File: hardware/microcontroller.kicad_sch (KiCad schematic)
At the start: 50 parts, among them J301 TC2050, J302 61300611121, J303 61300611121, J304 61300611121, J305 61300611121, J306 61300611121, J307 61300611121, Q301 BSS806NH, SW301 430182050816, SW302 430182050816, U301 STM32L552CET6, Y301 ECS-160-9-37-CKM-TR3, Y302 ABS05-32.768KHZ-9-T

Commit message: HW: Use 0201 where applicable
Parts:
- removed R319: 2.2 kΩ, perfect_footprints:R_0402_1005Metric, symbol Device:R
- added R305: 2.2 kΩ, perfect_footprints:R_0201_0603Metric, symbol Device:R
- C301, C302, C304, C305, C306, C307, C308, C309, C310, C311, C312, C313, C315: footprint perfect_footprints:C_0402_1005Metric -> perfect_footprints:C_0201_0603Metric; Size 0402 -> 0201
- C303, C314: value 4.7 µF -> 22 µF; footprint perfect_footprints:C_0402_1005Metric_HDI -> Capacitor_SMD:C_0603_1608Metric; Size 0402 -> 0603
- R301, R302: footprint perfect_footprints:R_0402_1005Metric -> perfect_footprints:R_0201_0603Metric; Power rating 0.1 W -> 0.05 W; Size 0402 -> 0201
- R303: renamed from R304; footprint perfect_footprints:R_0402_1005Metric -> perfect_footprints:R_0201_0603Metric; Power rating 0.1 W -> 0.05 W; Size 0402 -> 0201
- R304: renamed from R303; footprint perfect_footprints:R_0402_1005Metric -> perfect_footprints:R_0201_0603Metric; Power rating 0.1 W -> 0.05 W; Size 0402 -> 0201
- R306: renamed from R321; footprint perfect_footprints:R_0402_1005Metric -> perfect_footprints:R_0201_0603Metric; Power rating 0.1 W -> 0.05 W; Size 0402 -> 0201
- R307: renamed from R305; footprint perfect_footprints:R_0402_1005Metric -> perfect_footprints:R_0201_0603Metric; Power rating 0.1 W -> 0.05 W; Size 0402 -> 0201
- R308: renamed from R306; footprint perfect_footprints:R_0402_1005Metric -> perfect_footprints:R_0201_0603Metric; Power rating 0.1 W -> 0.05 W; Size 0402 -> 0201
- R309: renamed from R307; footprint perfect_footprints:R_0402_1005Metric -> perfect_footprints:R_0201_0603Metric; Power rating 0.1 W -> 0.05W; Size 0402 -> 0201
- R310: renamed from R308; footprint perfect_footprints:R_0402_1005Metric -> perfect_footprints:R_0201_0603Metric; Power rating 0.1 W -> 0.05W; Size 0402 -> 0201
- R311: renamed from R309; footprint perfect_footprints:R_0402_1005Metric -> perfect_footprints:R_0201_0603Metric; Power rating 0.1 W -> 0.05W; Size 0402 -> 0201
- R312: renamed from R310; footprint perfect_footprints:R_0402_1005Metric -> perfect_footprints:R_0201_0603Metric; Power rating 0.1 W -> 0.05W; Size 0402 -> 0201
- R313: renamed from R311; footprint perfect_footprints:R_0402_1005Metric -> perfect_footprints:R_0201_0603Metric; Power rating 0.1 W -> 0.05W; Size 0402 -> 0201
- R314: renamed from R312; footprint perfect_footprints:R_0402_1005Metric -> perfect_footprints:R_0201_0603Metric; Power rating 0.1 W -> 0.05W; Size 0402 -> 0201
- R315: renamed from R313; footprint perfect_footprints:R_0402_1005Metric -> perfect_footprints:R_0201_0603Metric; Power rating 0.1 W -> 0.05W; Size 0402 -> 0201
- R316: renamed from R314; footprint perfect_footprints:R_0402_1005Metric -> perfect_footprints:R_0201_0603Metric; Power rating 0.1 W -> 0.05W; Size 0402 -> 0201
- R317: renamed from R315; footprint perfect_footprints:R_0402_1005Metric -> perfect_footprints:R_0201_0603Metric; Power rating 0.1 W -> 0.05W; Size 0402 -> 0201
- R319: renamed from R317; footprint perfect_footprints:R_0402_1005Metric -> perfect_footprints:R_0201_0603Metric; Power rating 0.1 W -> 0.05W; Size 0402 -> 0201
- R320: renamed from R318; footprint perfect_footprints:R_0402_1005Metric -> perfect_footprints:R_0201_0603Metric; Power rating 0.1 W -> 0.05 W; Size 0402 -> 0201
- R321: renamed from R320; footprint perfect_footprints:R_0402_1005Metric -> perfect_footprints:R_0201_0603Metric; Power rating 0.1 W -> 0.05 W; Size 0402 -> 0201
- renumbered J304 to J303, J303 to J304, J306 to J305, J305 to J306, R316 to R318
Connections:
- net I2C.SCL: now also J307.3 (Pin_3), R305.2; no longer J307.5 (Pin_5)
- net I2C.SDA: now also J307.5 (Pin_5); no longer J307.3 (Pin_3)
- net V_3V3: now also R305.1
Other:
- note added: "Bulk + 1 µF x VDD pin"
- note removed: "4.7 µF + 1 µF x VDD pin"
- moved on the sheet: C301, C315, J304, J306, R303, R306, R319, SW301, SW302

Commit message: HW: Remove GPIO PA15 and PB2 for easier routing
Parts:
- removed J305: 61300611121, Connector_PinHeader_2.54mm:PinHeader_1x06_P2.54mm_Vertical, symbol Connector_Generic:Conn_01x06
- SW301, SW302: value 430182050816 -> PTS645S
- renumbered C310 to C309, C312 to C310, C313 to C311, C314 to C312, C309 to C313, C311 to C314, J307 to J302, J302 to J303, J303 to J305
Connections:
- net GPIO_PA5: no longer names the net of U301.15 (PA5)
- net GPIO_PB2: no longer names the net of U301.20 (PB2)
- no-connect marks 8 -> 10
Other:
- moved on the sheet: C301, C302, C303, C304, C305, C306, C307, C308, C309, C310, C311, C312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

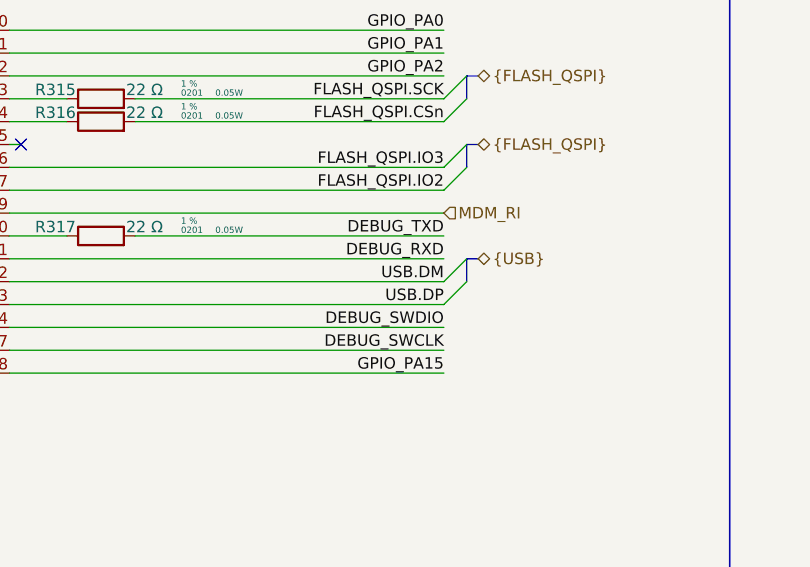
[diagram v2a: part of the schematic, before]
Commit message: HW: Fix BG77, relocate V_BAT bulk cap
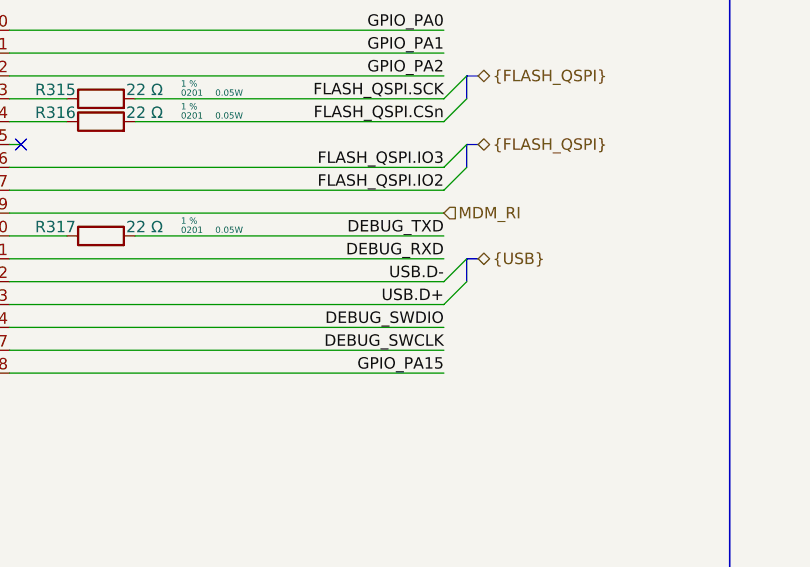
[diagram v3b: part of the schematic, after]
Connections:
- net USB.DM renamed USB.D-
- net USB.DP renamed USB.D+
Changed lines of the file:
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@@
 		)
 	)
-	(label "USB.DM"
+	(label "USB.D-"
 		(at 266.7 111.76 180)
 		(effects
@@
 		)
 	)
-	(label "USB.DP"
+	(label "USB.D+"
 		(at 266.7 114.3 180)
 		(effects

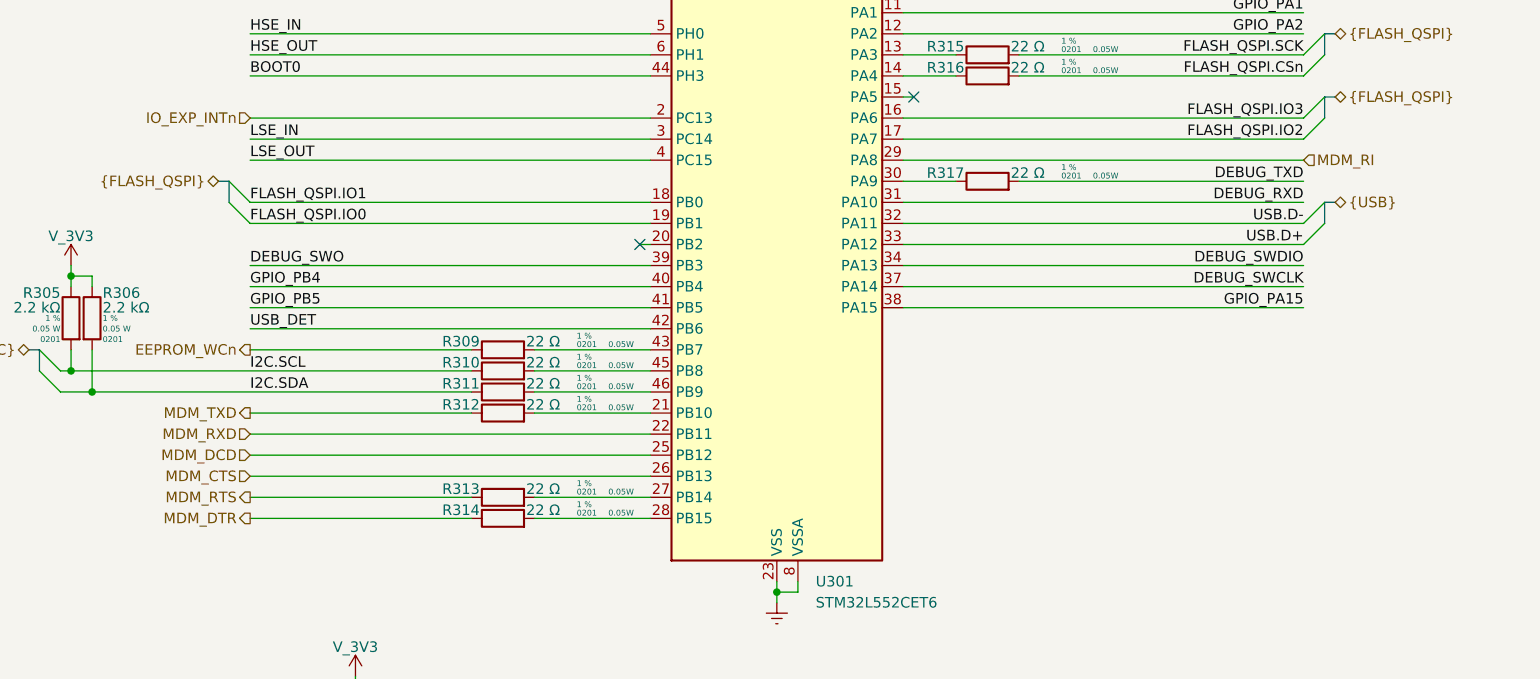
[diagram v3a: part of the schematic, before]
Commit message: HW: Replace BG77 with BG95
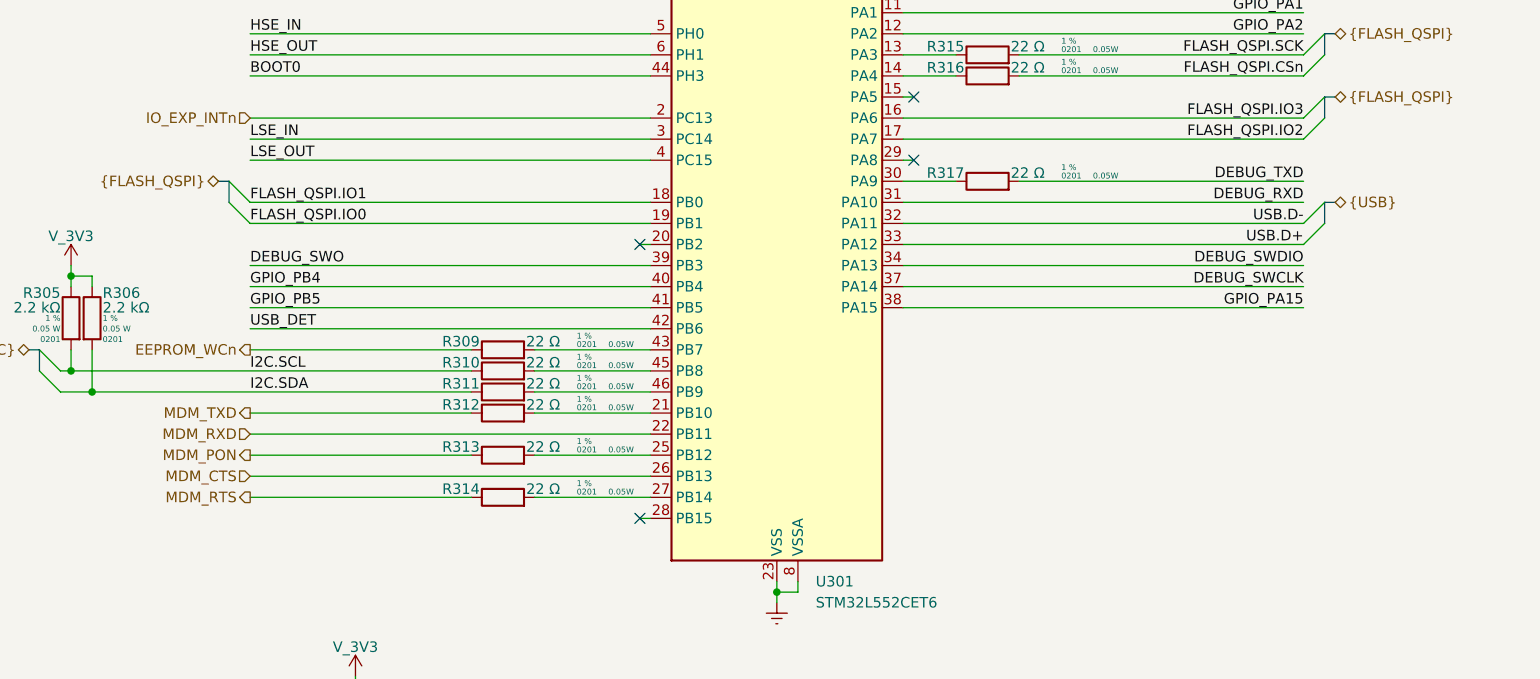
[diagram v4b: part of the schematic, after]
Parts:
- removed R314: 22 Ω, perfect_footprints:R_0201_0603Metric, symbol Device:R
- added R313: 22 Ω, perfect_footprints:R_0201_0603Metric, symbol Device:R
- renumbered R313 to R314
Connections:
- net MDM_DCD: no longer names the net of U301.25 (PB12)
- net MDM_DCD: now also R313.2
- net MDM_RI: no longer names the net of U301.29 (PA8)
- new net MDM_PON: R313.1
- no-connect marks 10 -> 12
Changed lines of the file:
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@@
 	)
 	(no_connect
+		(at 186.69 147.32)
+	)
+	(no_connect
 		(at 43.18 93.98)
 	)
@@
 	)
 	(no_connect
+		(at 219.71 104.14)
+	)
+	(no_connect
 		(at 387.35 97.79)
 	)
@@
 	(wire
 		(pts
-			(xy 173.99 147.32) (xy 187.96 147.32)
-		)
-		(stroke
-			(width 0)
-			(type default)
-		)
-	)
-	(wire
-		(pts
 			(xy 386.08 72.39) (xy 388.62 72.39)
 		)
@@
 	(wire
 		(pts
-			(xy 139.7 139.7) (xy 187.96 139.7)
-		)
-		(stroke
-			(width 0)
-			(type default)
-		)
-	)
-	(wire
-		(pts
 			(xy 254 76.2) (xy 254 77.47)
 		)
@@
 	(wire
 		(pts
+			(xy 139.7 139.7) (xy 166.37 139.7)
+		)
+		(stroke
+			(width 0)
+			(type default)
+		)
+	)
+	(wire
+		(pts
 			(xy 152.4 76.2) (xy 165.1 76.2)
 		)
@@
 	(wire
 		(pts
-			(xy 139.7 147.32) (xy 166.37 147.32)
+			(xy 120.65 127) (xy 120.65 132.08)
 		)
 		(stroke
@@
 	(wire
 		(pts
-			(xy 120.65 127) (xy 120.65 132.08)
+			(xy 190.5 73.66) (xy 190.5 76.2)
 		)
 		(stroke
@@
 	(wire
 		(pts
-			(xy 190.5 73.66) (xy 190.5 76.2)
+			(xy 186.69 147.32) (xy 187.96 147.32)
 		)
 		(stroke
@@
 	(wire
 		(pts
-			(xy 218.44 104.14) (xy 266.7 104.14)
-		)
-		(stroke
-			(width 0)
-			(type default)
-		)
-	)
-	(wire
-		(pts
 			(xy 337.82 67.31) (xy 335.28 67.31)
 		)
@@
 	(wire
 		(pts
+			(xy 173.99 139.7) (xy 187.96 139.7)
+		)
+		(stroke
+			(width 0)
+			(type default)
+		)
+	)
+	(wire
+		(pts
 			(xy 264.16 177.8) (xy 266.7 177.8)
 		)
@@
 	(wire
 		(pts
+			(xy 218.44 104.14) (xy 219.71 104.14)
+		)
+		(stroke
+			(width 0)
+			(type default)
+		)
+	)
+	(wire
+		(pts
 			(xy 218.44 86.36) (xy 266.7 86.36)
 		)
@@
 		)
 	)
-	(hierarchical_label "MDM_DTR"
+	(hierarchical_label "MDM_PON"
 		(shape output)
-		(at 139.7 147.32 180)
+		(at 139.7 139.7 180)
 		(effects
 			(font
@@
 		)
 	)
-	(hierarchical_label "MDM_DCD"
-		(shape input)
-		(at 139.7 139.7 180)
-		(effects
-			(font
-				(size 1.27 1.27)
-			)
-			(justify right)
-		)
-	)
 	(hierarchical_label "{I2C}"
 		(shape bidirectional)
@@
 		)
 	)
-	(hierarchical_label "MDM_RI"
-		(shape input)
-		(at 266.7 104.14 0)
-		(effects
-			(font
-				(size 1.27 1.27)
-			)
-			(justify left)
-		)
-	)
 	(hierarchical_label "MDM_RTS"
 		(shape output)
@@
 	)
 	(symbol
-		(lib_id "Device:R")
-		(at 170.18 147.32 90)
-		(unit 1)
-		(body_style 1)
-		(exclude_from_sim no)
-		(in_bom yes)
-		(on_board yes)
-		(in_pos_files yes)
-		(dnp no)
-		(property "Reference" "R314"
-			(at 167.386 147.066 90)
-			(show_name no)
-			(do_not_autoplace no)
-			(effects
-				(font
-					(size 1.27 1.27)
-				)
-				(justify left top)
-			)
-		)
-		(property "Value" "22 Ω"
-			(at 172.974 147.066 90)
-			(show_name no)
-			(do_not_autoplace no)
-			(effects
-				(font
-					(size 1.27 1.27)
-				)
-				(justify right top)
-			)
-		)
-		(property "Footprint" "perfect_footprints:R_0201_0603Metric"
-			(at 170.18 149.098 90)
-			(hide yes)
-			(show_name no)
-			(do_not_autoplace no)
-			(effects
-				(font
-					(size 1.27 1.27)
-				)
-			)
-		)
-		(property "Datasheet" ""
-			(at 170.18 147.32 0)
-			(hide yes)
-			(show_name no)
-			(do_not_autoplace no)
-			(effects
-				(font
-					(size 1.27 1.27)
-				)
-			)
-		)
-		(property "Description" "22Ω Resistor 1% 0.05W 0201"
-			(at 170.18 147.32 0)
-			(hide yes)
-			(show_name no)
-			(do_not_autoplace no)
-			(effects
-				(font
-					(size 1.27 1.27)
-				)
-			)
-		)
-		(property "Tolerance" "1 %"
-			(at 179.07 146.05 90)
-			(show_name no)
-			(do_not_autoplace no)
-			(effects
-				(font
-					(size 0.7 0.7)
-				)
-				(justify right top)
-			)
-		)
-		(property "Power rating" "0.05W"
-			(at 182.88 147.066 90)
-			(show_name no)
-			(do_not_autoplace no)
-			(effects
-				(font
-					(size 0.7 0.7)
-				)
-				(justify right top)
-			)
-		)
-		(property "Size" "0201"
-			(at 179.07 147.066 90)
-			(show_name no)
-			(do_not_autoplace no)
-			(effects
-				(font
-					(size 0.7 0.7)
-				)
-				(justify right top)
-			)
-		)
-		(pin "2"
-		)
-		(pin "1"
-		)
-		(instances
-			(project "iida_devkit"
-				(path "/b12a6e25-97fb-4aba-bc96-af8db389bb9a/6dd8d741-3080-458c-a4f5-a05a3905bb8a"
-					(reference "R314")
-					(unit 1)
-				)
-			)
-		)
-	)
-	(symbol
 		(lib_id "Connector_Generic:Conn_01x06")
 		(at 368.3 97.79 0)
@@
 		(in_pos_files yes)
 		(dnp no)
-		(property "Reference" "R313"
+		(property "Reference" "R314"
 			(at 167.386 144.526 90)
 			(show_name no)
@@
 			(project "iida_devkit"
 				(path "/b12a6e25-97fb-4aba-bc96-af8db389bb9a/6dd8d741-3080-458c-a4f5-a05a3905bb8a"
-					(reference "R313")
+					(reference "R314")
 					(unit 1)
 				)
@@
 					(unit 1)
 				)
+			)
+		)
+	)
+	(symbol
+		(lib_id "Device:R")
+		(at 170.18 139.7 90)
+		(unit 1)
+		(body_style 1)
+		(exclude_from_sim no)
+		(in_bom yes)
+		(on_board yes)
+		(in_pos_files yes)
+		(dnp no)
+		(property "Reference" "R313"
+			(at 167.386 139.446 90)
+			(show_name no)
+			(do_not_autoplace no)
+			(effects
+				(font
+					(size 1.27 1.27)
+				)
+				(justify left top)
+			)
+		)
+		(property "Value" "22 Ω"
+			(at 172.974 139.446 90)
+			(show_name no)
+			(do_not_autoplace no)
+			(effects
+				(font
+					(size 1.27 1.27)
+				)
+				(justify right top)
+			)
+		)
+		(property "Footprint" "perfect_footprints:R_0201_0603Metric"
+			(at 170.18 141.478 90)
+			(hide yes)
+			(show_name no)
+			(do_not_autoplace no)
+			(effects
+				(font
+					(size 1.27 1.27)
+				)
+			)
+		)
+		(property "Datasheet" ""
+			(at 170.18 139.7 0)
+			(hide yes)
+			(show_name no)
+			(do_not_autoplace no)
+			(effects
+				(font
+					(size 1.27 1.27)
+				)
+			)
+		)
+		(property "Description" "22Ω Resistor 1% 0.05W 0201"
+			(at 170.18 139.7 0)
+			(hide yes)
+			(show_name no)
+			(do_not_autoplace no)
+			(effects
+				(font
+					(size 1.27 1.27)
+				)
+			)
+		)
+		(property "Tolerance" "1 %"
+			(at 179.07 138.43 90)
+			(show_name no)
+			(do_not_autoplace no)
+			(effects
+				(font
+					(size 0.7 0.7)
+				)
+				(justify right top)
+			)
+		)
+		(property "Power rating" "0.05W"
+			(at 182.88 139.446 90)
+			(show_name no)
+			(do_not_autoplace no)
+			(effects
+				(font
+					(size 0.7 0.7)
+				)
+				(justify right top)
+			)
+		)
+		(property "Size" "0201"
+			(at 179.07 139.446 90)
+			(show_name no)
+			(do_not_autoplace no)
+			(effects
+				(font
+					(size 0.7 0.7)
+				)
+				(justify right top)
+			)
+		)
+		(pin "2"
+		)
+		(pin "1"
+		)
+		(instances
+			(project "iida_devkit"
+				(path "/b12a6e25-97fb-4aba-bc96-af8db389bb9a/6dd8d741-3080-458c-a4f5-a05a3905bb8a"
+					(reference "R313")
+					(unit 1)
+				)

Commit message: HW: Start interconnects
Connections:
- net GPIO_PB4: now also J303.3 (Pin_3); no longer J303.1 (Pin_1)
- net GPIO_PB5: now also J303.1 (Pin_1); no longer J303.3 (Pin_3)
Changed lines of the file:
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@@
 	)
 	(label "GPIO_PB5"
-		(at 349.25 69.85 0)
+		(at 349.25 64.77 0)
 		(effects
 			(font
@@
 	)
 	(label "GPIO_PB4"
-		(at 349.25 64.77 0)
+		(at 349.25 69.85 0)
 		(effects
 			(font
